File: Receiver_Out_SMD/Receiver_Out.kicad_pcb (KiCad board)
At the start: 2 copper layers, 59.3 x 71.4 mm, 47 parts, among them J1 String1, J2 String2, J3 String3, J4 String4, J5 PGM, J6 VIN_Voltage, J7 RJ45, J8 Conn_ARM_SWD_TagConnect_TC203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, SW1 Test, U2 AMS1117-5.0, U3 AM26C32IN, U4 74HCT541, U5 ATtiny1616-M

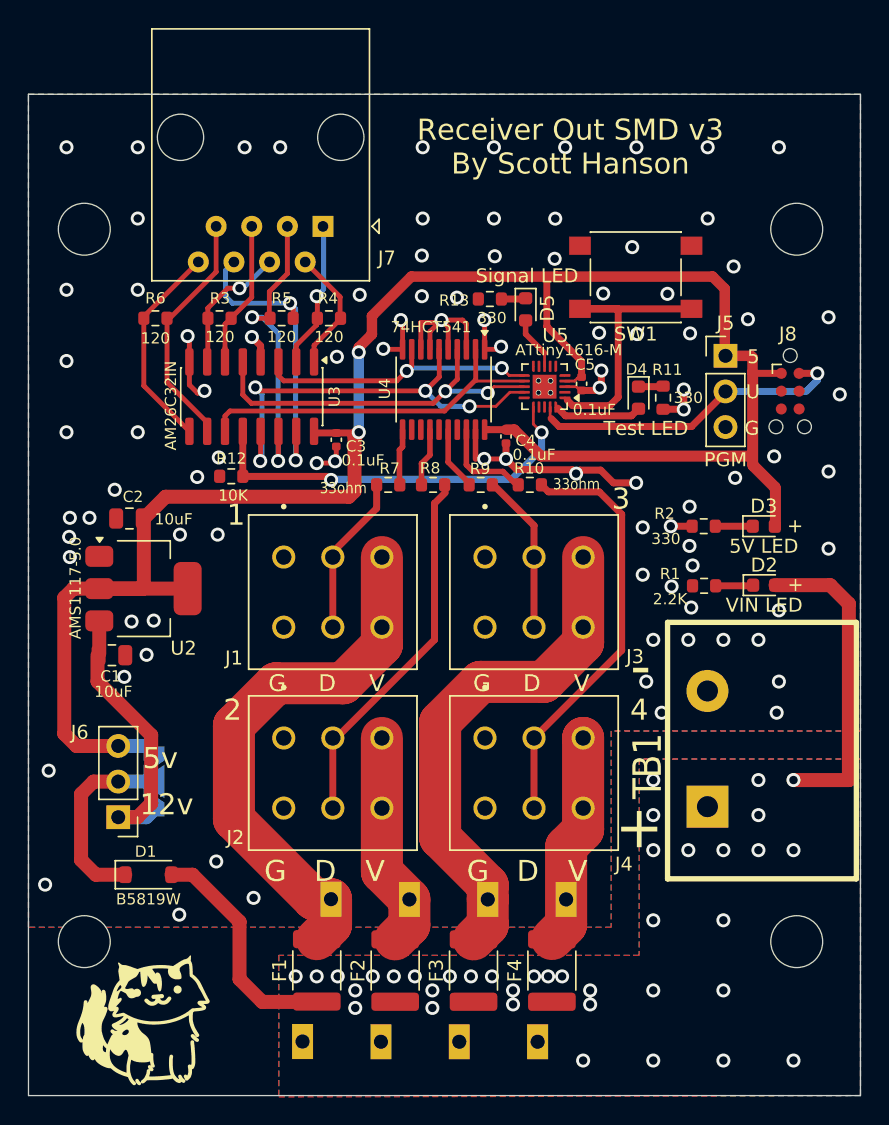
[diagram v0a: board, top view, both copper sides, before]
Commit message: receiver improve silkscreen
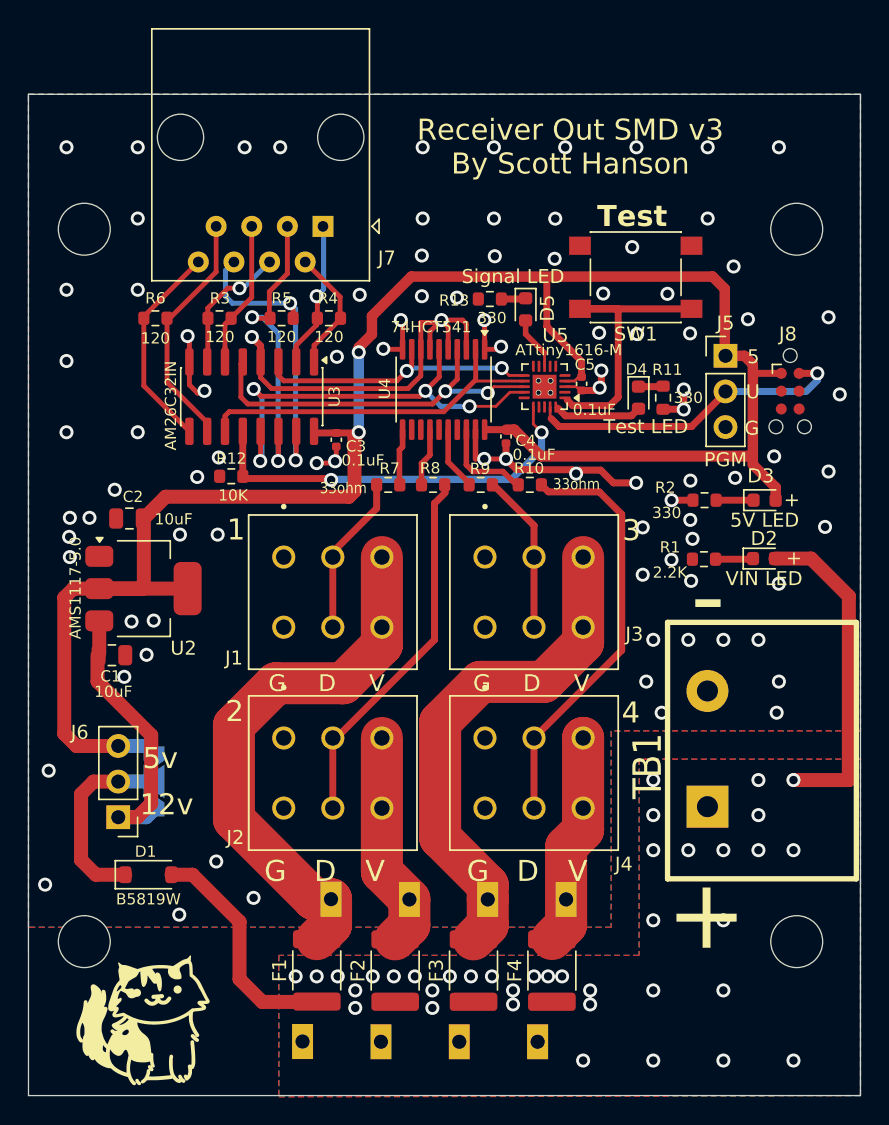
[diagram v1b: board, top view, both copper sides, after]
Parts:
- moved D2 1.90 mm to (121.2, 114.9)
- moved R1 1.90 mm to (116.9, 115.0)
- moved D3 1.86 mm to (121.2, 110.8)
- moved R2 1.86 mm to (117.0, 110.8)
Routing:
- net GND: track 51.8 -> 66.9 mm
- net +5V: track 170.9 -> 157.0 mm
- net VIN1: track 38.8 -> 39.9 mm
